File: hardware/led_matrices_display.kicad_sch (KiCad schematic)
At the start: 4 parts, among them U10 KWM-20882CUYB, U11 KWM-20882CUYB, U12 KWM-20882CUYB, U13 KWM-20882CUYB

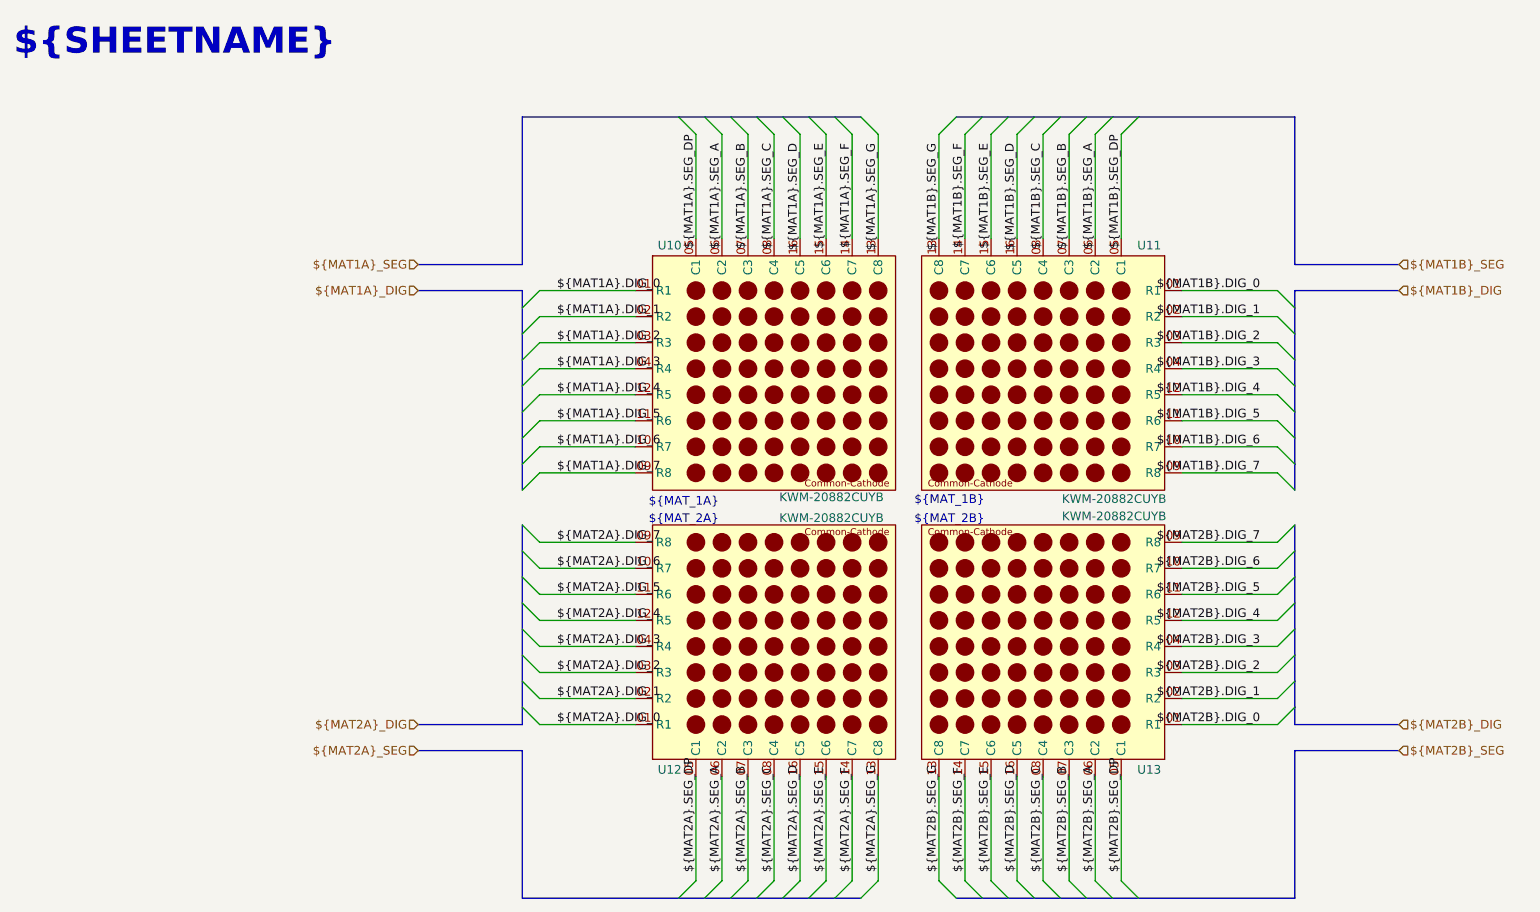
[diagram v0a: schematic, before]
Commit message: Completed the property teble except for the cyristal oscilator
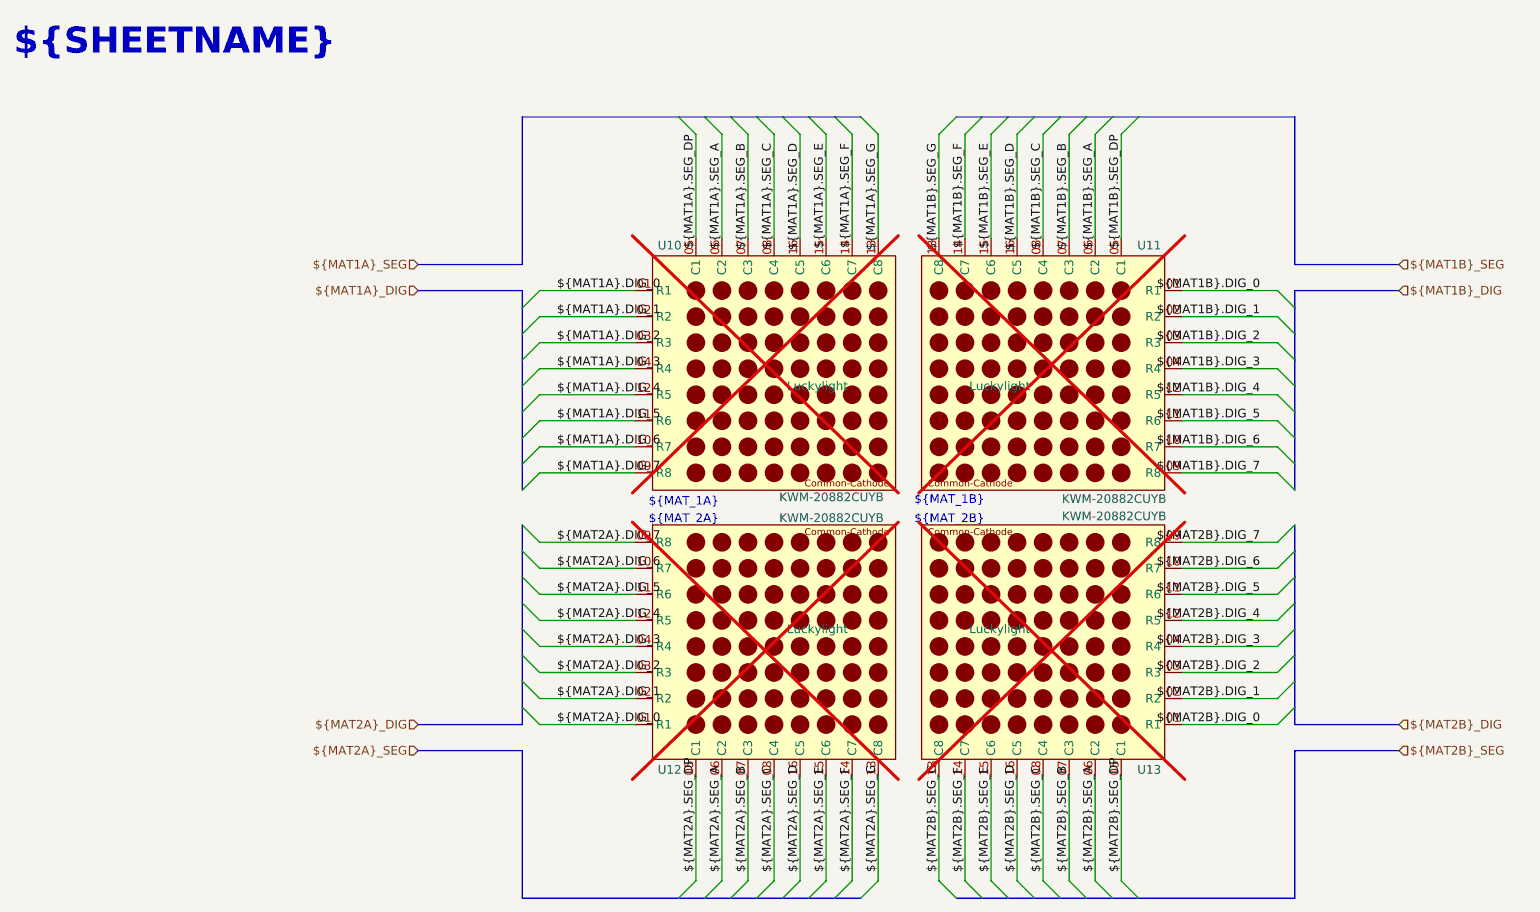
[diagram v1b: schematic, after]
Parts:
- U10, U11, U12, U13: Manuf. Name (none) -> Luckylight; Supplier Unit Price 75,00 kr -> $7.0000; now not fitted; now left out of the parts list
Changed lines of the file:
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@@
 		(unit 1)
 		(exclude_from_sim no)
-		(in_bom yes)
+		(in_bom no)
 		(on_board yes)
-		(dnp no)
+		(dnp yes)
 		(property "Reference" "U13"
 			(at 186.182 128.524 0)
@@
 			)
 		)
-		(property "Supplier Unit Price" "75,00 kr"
+		(property "Supplier Unit Price" " $7.0000"
 			(at 162.56 107.95 0)
 			(effects
@@
 				)
 				(hide yes)
+			)
+		)
+		(property "Manuf. Name" "Luckylight"
+			(at 162.56 107.95 0)
+			(effects
+				(font
+					(size 1.27 1.27)
+				)
 			)
 		)
@@
 		(unit 1)
 		(exclude_from_sim no)
-		(in_bom yes)
+		(in_bom no)
 		(on_board yes)
-		(dnp no)
+		(dnp yes)
 		(property "Reference" "U11"
 			(at 186.182 51.816 0)
@@
 			)
 		)
-		(property "Supplier Unit Price" "75,00 kr"
+		(property "Supplier Unit Price" " $7.0000"
 			(at 162.56 72.39 0)
 			(effects
@@
 				)
 				(hide yes)
+			)
+		)
+		(property "Manuf. Name" "Luckylight"
+			(at 162.56 72.39 0)
+			(effects
+				(font
+					(size 1.27 1.27)
+				)
 			)
 		)
@@
 		(unit 1)
 		(exclude_from_sim no)
-		(in_bom yes)
+		(in_bom no)
 		(on_board yes)
-		(dnp no)
+		(dnp yes)
 		(property "Reference" "U12"
 			(at 112.522 128.524 0)
@@
 			)
 		)
-		(property "Supplier Unit Price" "75,00 kr"
+		(property "Supplier Unit Price" " $7.0000"
 			(at 135.89 107.95 0)
 			(effects
@@
 				)
 				(hide yes)
+			)
+		)
+		(property "Manuf. Name" "Luckylight"
+			(at 135.89 107.95 0)
+			(effects
+				(font
+					(size 1.27 1.27)
+				)
 			)
 		)
@@
 		(unit 1)
 		(exclude_from_sim no)
-		(in_bom yes)
+		(in_bom no)
 		(on_board yes)
-		(dnp no)
+		(dnp yes)
 		(property "Reference" "U10"
 			(at 112.522 51.816 0)
@@
 			)
 		)
-		(property "Supplier Unit Price" "75,00 kr"
+		(property "Supplier Unit Price" " $7.0000"
 			(at 135.89 72.39 0)
 			(effects
@@
 			)
 		)
+		(property "Manuf. Name" "Luckylight"
+			(at 135.89 72.39 0)
+			(effects
+				(font
+					(size 1.27 1.27)
+				)
+			)
+		)

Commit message: Made some small changes on the properties of some components while having last weeks meeting and added the fp-info-cache to the gitignore file
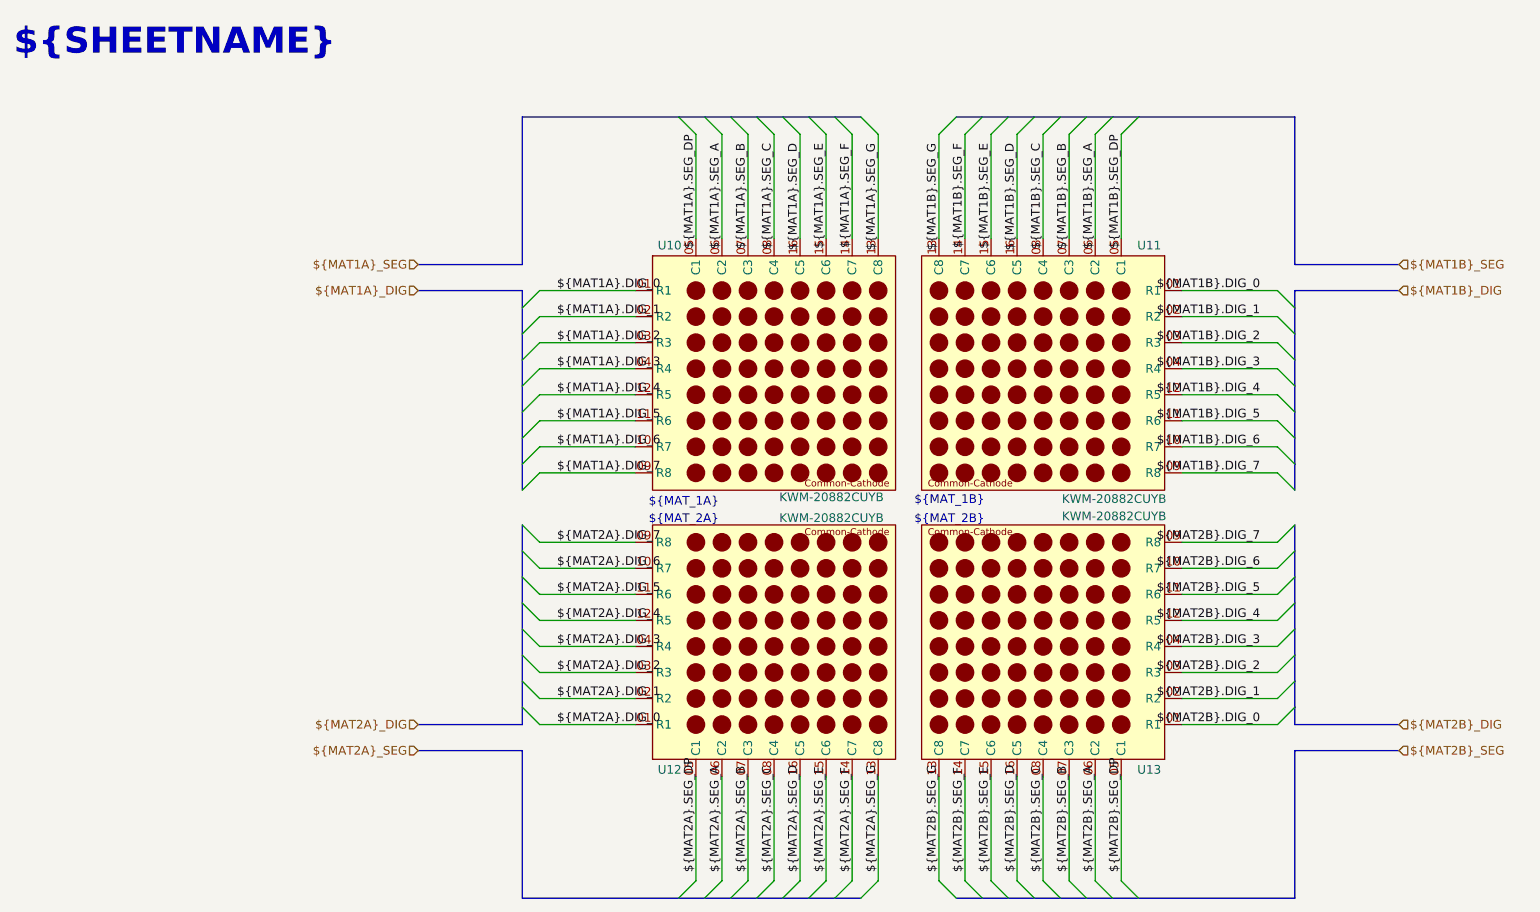
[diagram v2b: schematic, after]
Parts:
- U10, U11, U12, U13: now fitted
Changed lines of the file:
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@@
 		(in_bom no)
 		(on_board yes)
-		(dnp yes)
+		(dnp no)
 		(property "Reference" "U13"
 			(at 186.182 128.524 0)
@@
 					(size 1.27 1.27)
 				)
+				(hide yes)
 			)
 		)
@@
 		(in_bom no)
 		(on_board yes)
-		(dnp yes)
+		(dnp no)
 		(property "Reference" "U11"
 			(at 186.182 51.816 0)
@@
 					(size 1.27 1.27)
 				)
+				(hide yes)
 			)
 		)
@@
 		(in_bom no)
 		(on_board yes)
-		(dnp yes)
+		(dnp no)
 		(property "Reference" "U12"
 			(at 112.522 128.524 0)
@@
 					(size 1.27 1.27)
 				)
+				(hide yes)
 			)
 		)
@@
 		(in_bom no)
 		(on_board yes)
-		(dnp yes)
+		(dnp no)
 		(property "Reference" "U10"
 			(at 112.522 51.816 0)
@@
 					(size 1.27 1.27)
 				)
-			)
-		)
+				(hide yes)
+			)
+		)

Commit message: Electric Rules Check completed.
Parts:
- U10, U11, U12, U13: footprint Project-kitchen_timer:KWM-20882CUYB -> kitchen_timer:KWM-20882CUYB
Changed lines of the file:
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@@
 		)
 	)
-	(hierarchical_label "${MAT1B}_SEG"
+	(hierarchical_label "${MAT1B}{SEG}"
 		(shape input)
 		(at 220.98 54.61 0)
@@
 		)
 	)
-	(hierarchical_label "${MAT1A}_SEG"
+	(hierarchical_label "${MAT1A}{SEG}"
 		(shape input)
 		(at 77.47 54.61 180)
@@
 		)
 	)
-	(hierarchical_label "${MAT2A}_DIG"
+	(hierarchical_label "${MAT2A}{DIG}"
 		(shape input)
 		(at 77.47 121.92 180)
@@
 		)
 	)
-	(hierarchical_label "${MAT2B}_DIG"
+	(hierarchical_label "${MAT2B}{DIG}"
 		(shape input)
 		(at 220.98 121.92 0)
@@
 		)
 	)
-	(hierarchical_label "${MAT1A}_DIG"
+	(hierarchical_label "${MAT1A}{DIG}"
 		(shape input)
 		(at 77.47 58.42 180)
@@
 		)
 	)
-	(hierarchical_label "${MAT2A}_SEG"
+	(hierarchical_label "${MAT2A}{SEG}"
 		(shape input)
 		(at 77.47 125.73 180)
@@
 		)
 	)
-	(hierarchical_label "${MAT2B}_SEG"
+	(hierarchical_label "${MAT2B}{SEG}"
 		(shape input)
 		(at 220.98 125.73 0)
@@
 		)
 	)
-	(hierarchical_label "${MAT1B}_DIG"
+	(hierarchical_label "${MAT1B}{DIG}"
 		(shape input)
 		(at 220.98 58.42 0)
@@
 			)
 		)
-		(property "Footprint" "Project-kitchen_timer:KWM-20882CUYB"
+		(property "Footprint" "kitchen_timer:KWM-20882CUYB"
 			(at 171.45 111.76 0)
 			(effects
@@
 			)
 		)
-		(property "Footprint" "Project-kitchen_timer:KWM-20882CUYB"
+		(property "Footprint" "kitchen_timer:KWM-20882CUYB"
 			(at 171.45 68.58 0)
 			(effects
@@
 		)
 		(property "Manuf. Name" "Luckylight"
+			(at 162.56 72.39 0)
+			(effects
+				(font
+					(size 1.27 1.27)
+				)
+				(hide yes)
+			)
+		)
+		(property "Part Num" ""
+			(at 162.56 72.39 0)
+			(effects
+				(font
+					(size 1.27 1.27)
+				)
+				(hide yes)
+			)
+		)
+		(property "Supplier Part #" ""
 			(at 162.56 72.39 0)
 			(effects
@@
 			)
 		)
-		(property "Footprint" "Project-kitchen_timer:KWM-20882CUYB"
+		(property "Footprint" "kitchen_timer:KWM-20882CUYB"
 			(at 127 111.76 0)
 			(effects
@@
 			)
 		)
-		(property "Footprint" "Project-kitchen_timer:KWM-20882CUYB"
+		(property "Footprint" "kitchen_timer:KWM-20882CUYB"
 			(at 127 68.58 0)
 			(effects

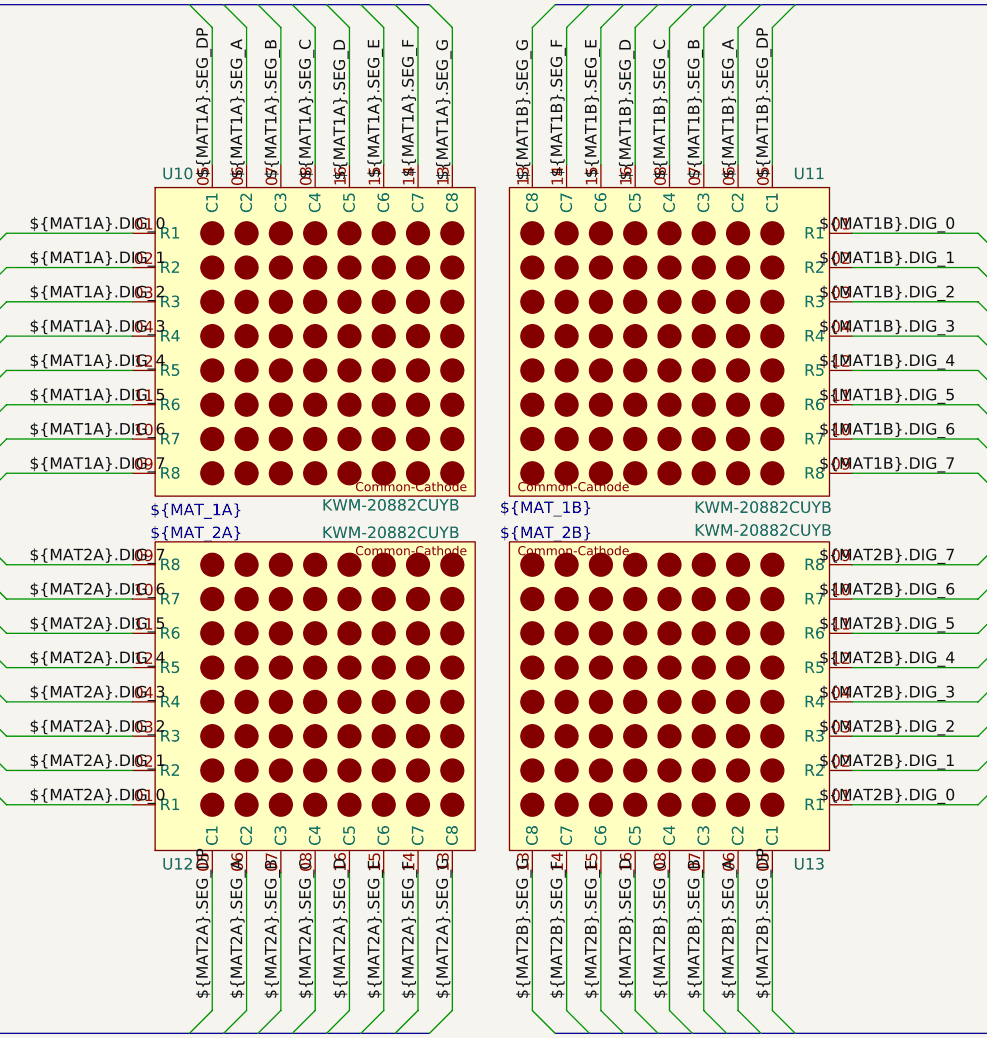
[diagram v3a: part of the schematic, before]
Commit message: Added footprints to mounting holes and selected a part for the test LED.
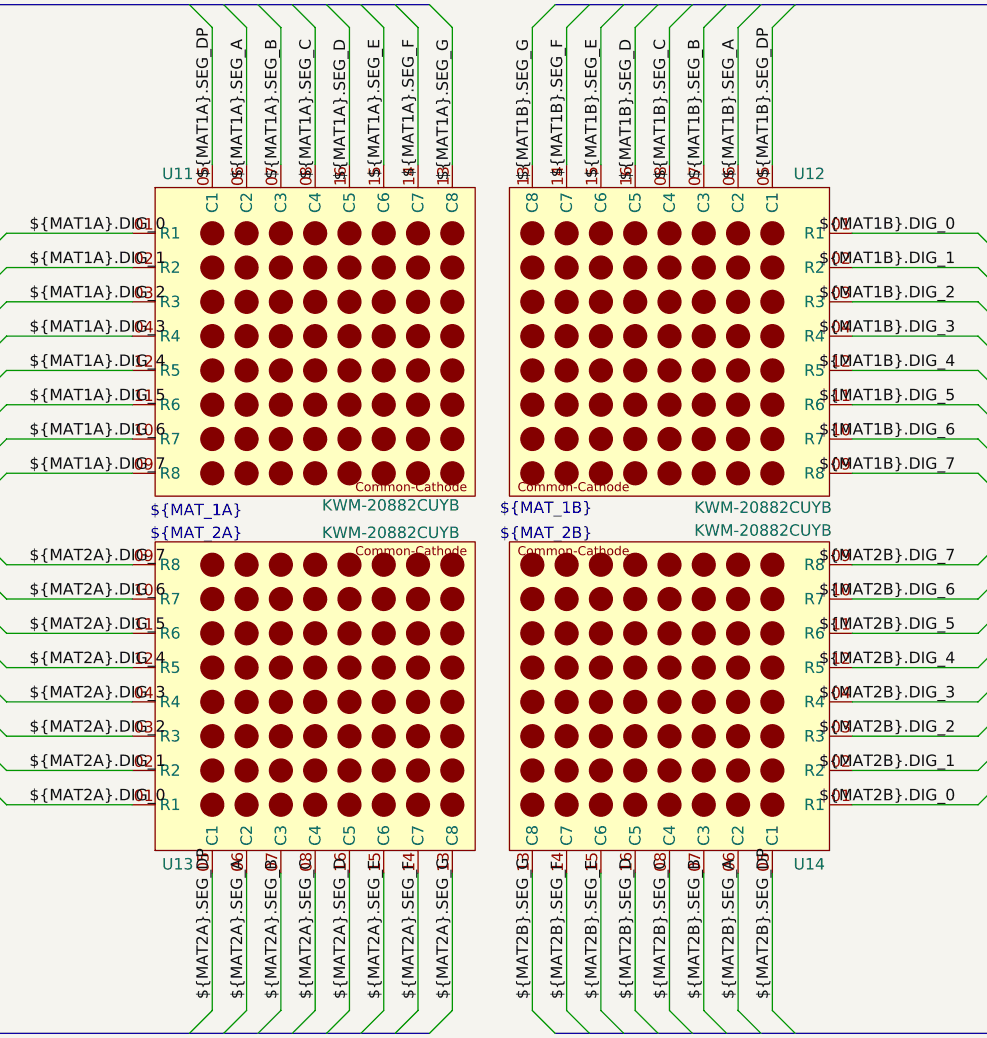
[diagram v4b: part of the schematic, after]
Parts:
- renumbered U10 to U11, U11 to U12, U12 to U13, U13 to U14
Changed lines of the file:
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@@
 		(on_board yes)
 		(dnp no)
-		(property "Reference" "U13"
+		(property "Reference" "U14"
 			(at 186.182 128.524 0)
 			(effects
@@
 				)
 				(hide yes)
+			)
+		)
+		(property "Manufacturer_Name" ""
+			(at 162.56 107.95 0)
+			(effects
+				(font
+					(size 1.27 1.27)
+				)
+			)
+		)
+		(property "Manufacturer_Part_Number" ""
+			(at 162.56 107.95 0)
+			(effects
+				(font
+					(size 1.27 1.27)
+				)
+			)
+		)
+		(property "Mouser Part Number" ""
+			(at 162.56 107.95 0)
+			(effects
+				(font
+					(size 1.27 1.27)
+				)
+			)
+		)
+		(property "Mouser Price/Stock" ""
+			(at 162.56 107.95 0)
+			(effects
+				(font
+					(size 1.27 1.27)
+				)
 			)
 		)
@@
 			(project "kitchen_timer-hardware"
 				(path "/8963deea-96bc-4401-b671-98fbe9ed9c6a/51b07aee-e177-4be7-b84e-75e5e68b78bc"
-					(reference "U13")
+					(reference "U14")
 					(unit 1)
 				)
@@
 		(on_board yes)
 		(dnp no)
-		(property "Reference" "U11"
+		(property "Reference" "U12"
 			(at 186.182 51.816 0)
 			(effects
@@
 				)
 				(hide yes)
+			)
+		)
+		(property "Manufacturer_Name" ""
+			(at 162.56 72.39 0)
+			(effects
+				(font
+					(size 1.27 1.27)
+				)
+			)
+		)
+		(property "Manufacturer_Part_Number" ""
+			(at 162.56 72.39 0)
+			(effects
+				(font
+					(size 1.27 1.27)
+				)
+			)
+		)
+		(property "Mouser Part Number" ""
+			(at 162.56 72.39 0)
+			(effects
+				(font
+					(size 1.27 1.27)
+				)
+			)
+		)
+		(property "Mouser Price/Stock" ""
+			(at 162.56 72.39 0)
+			(effects
+				(font
+					(size 1.27 1.27)
+				)
 			)
 		)
@@
 			(project "kitchen_timer-hardware"
 				(path "/8963deea-96bc-4401-b671-98fbe9ed9c6a/51b07aee-e177-4be7-b84e-75e5e68b78bc"
-					(reference "U11")
+					(reference "U12")
 					(unit 1)
 				)
@@
 		(on_board yes)
 		(dnp no)
-		(property "Reference" "U12"
+		(property "Reference" "U13"
 			(at 112.522 128.524 0)
 			(effects
@@
 				)
 				(hide yes)
+			)
+		)
+		(property "Manufacturer_Name" ""
+			(at 135.89 107.95 0)
+			(effects
+				(font
+					(size 1.27 1.27)
+				)
+			)
+		)
+		(property "Manufacturer_Part_Number" ""
+			(at 135.89 107.95 0)
+			(effects
+				(font
+					(size 1.27 1.27)
+				)
+			)
+		)
+		(property "Mouser Part Number" ""
+			(at 135.89 107.95 0)
+			(effects
+				(font
+					(size 1.27 1.27)
+				)
+			)
+		)
+		(property "Mouser Price/Stock" ""
+			(at 135.89 107.95 0)
+			(effects
+				(font
+					(size 1.27 1.27)
+				)
 			)
 		)
@@
 			(project "kitchen_timer-hardware"
 				(path "/8963deea-96bc-4401-b671-98fbe9ed9c6a/51b07aee-e177-4be7-b84e-75e5e68b78bc"
-					(reference "U12")
+					(reference "U13")
 					(unit 1)
 				)
@@
 		(on_board yes)
 		(dnp no)
-		(property "Reference" "U10"
+		(property "Reference" "U11"
 			(at 112.522 51.816 0)
 			(effects
@@
 				)
 				(hide yes)
+			)
+		)
+		(property "Manufacturer_Name" ""
+			(at 135.89 72.39 0)
+			(effects
+				(font
+					(size 1.27 1.27)
+				)
+			)
+		)
+		(property "Manufacturer_Part_Number" ""
+			(at 135.89 72.39 0)
+			(effects
+				(font
+					(size 1.27 1.27)
+				)
+			)
+		)
+		(property "Mouser Part Number" ""
+			(at 135.89 72.39 0)
+			(effects
+				(font
+					(size 1.27 1.27)
+				)
+			)
+		)
+		(property "Mouser Price/Stock" ""
+			(at 135.89 72.39 0)
+			(effects
+				(font
+					(size 1.27 1.27)
+				)
 			)
 		)
@@
 			(project ""
 				(path "/8963deea-96bc-4401-b671-98fbe9ed9c6a/51b07aee-e177-4be7-b84e-75e5e68b78bc"
-					(reference "U10")
+					(reference "U11")
 					(unit 1)
 				)
